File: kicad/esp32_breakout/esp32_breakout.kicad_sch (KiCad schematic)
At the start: 26 parts, among them J1 JST B5B-PH-K-S, J10 JST B6B-PH-K-S, J2 JST B5B-PH-K-S, J3 JST B7B-PH-K-S, J4 XT30U-M, J5 HDR 8p M VERT 2.54mm, J6 JST B5B-ZR, J9 JST B6B-PH-K-S, SW1 SS12D10, U1 ESP32 DEV KIT Module 30-pin, U2 LM2596 Module

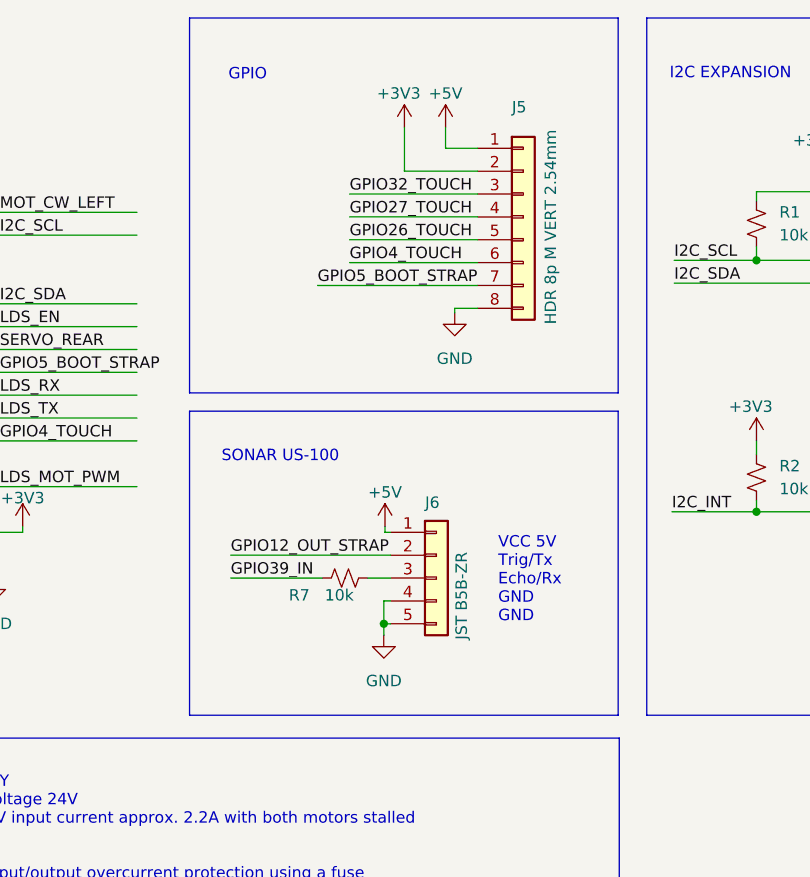
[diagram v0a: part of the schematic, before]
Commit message: Single GPIO header
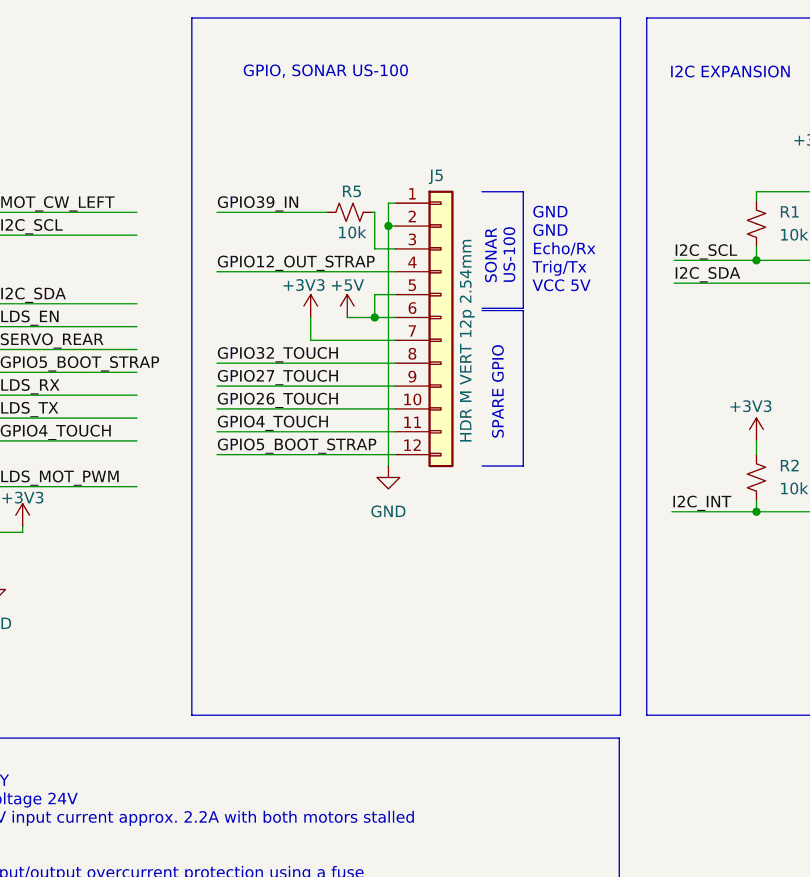
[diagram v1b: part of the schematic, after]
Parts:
- removed J5: HDR 8p M VERT 2.54mm, Connector_PinHeader_2.54mm:PinHeader_1x08_P2.54mm_Vertical, symbol Connector_Generic:Conn_01x08
- removed J6: JST B5B-ZR, Makerspet:JST_ZH_B5B-ZR_1x05_P1.50mm_Vertical, symbol Connector_Generic:Conn_01x05
- removed R7: 10k, Resistor_SMD:R_0603_1608Metric, symbol Device:R_Small_US
- added J5: HDR M VERT 12p 2.54mm, Connector_PinSocket_2.54mm:PinSocket_1x12_P2.54mm_Vertical, symbol Connector_Generic:Conn_01x12
- added R5: 10k, Resistor_SMD:R_0603_1608Metric, symbol Device:R_Small_US
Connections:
- net +3V3: now also J5.7 (Pin_7)
- net +5V: now also J5.5 (Pin_5), J5.6 (Pin_6)
- net GND: now also J5.1 (Pin_1), J5.2 (Pin_2)
- net GPIO12_OUT_STRAP: now also J5.4 (Pin_4)
- net GPIO26_TOUCH: now also J5.10 (Pin_10)
- net GPIO27_TOUCH: now also J5.9 (Pin_9)
- net GPIO32_TOUCH: now also J5.8 (Pin_8)
- net GPIO39_IN: now also R5.1
- net GPIO4_TOUCH: now also J5.11 (Pin_11)
- net GPIO5_BOOT_STRAP: now also J5.12 (Pin_12)
- new net: J5.3 (Pin_3), R5.2
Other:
- note added: "GND GND Echo/Rx Trig/Tx VCC 5V"
- note added: "GPIO, SONAR US-100"
- note added: "SPARE GPIO"
- note removed: "GPIO"
- note removed: "VCC 5V Trig/Tx Echo/Rx GND GND"

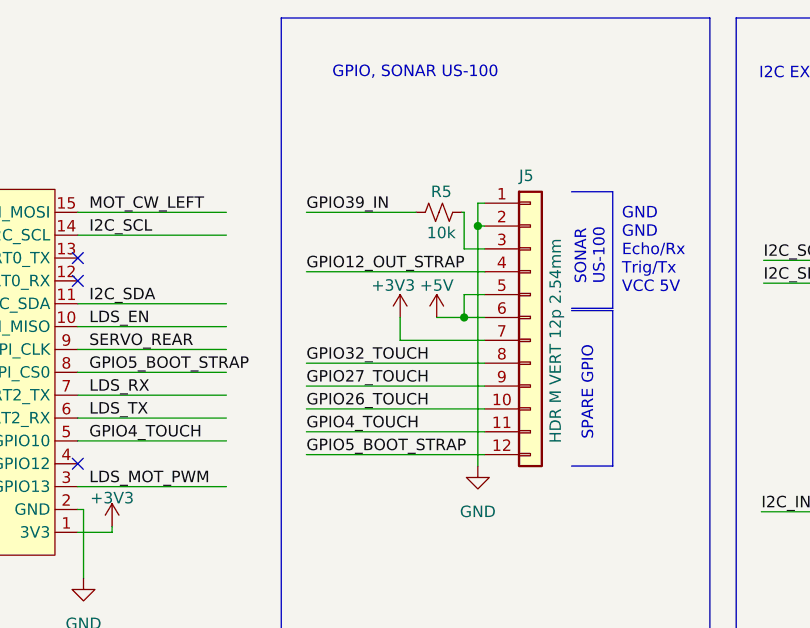
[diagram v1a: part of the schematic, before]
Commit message: PCB hole, sonar tweaks
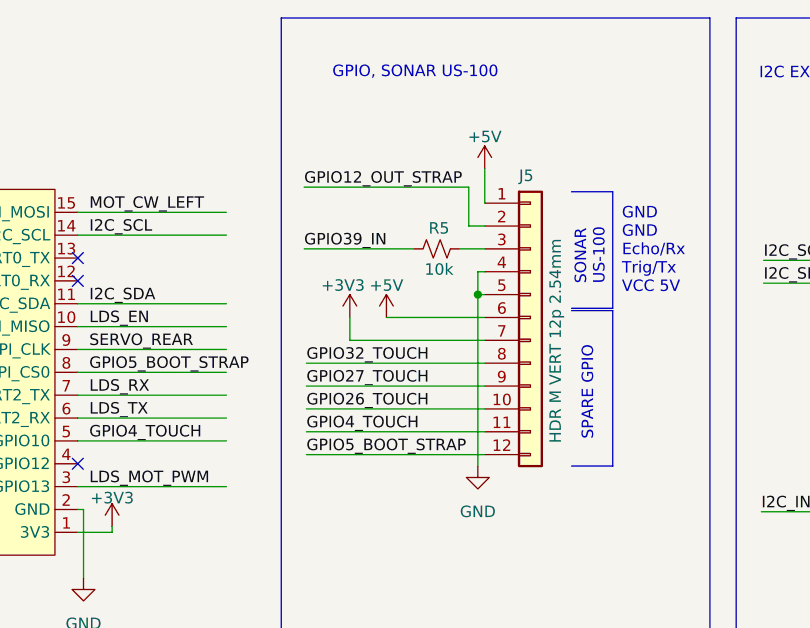
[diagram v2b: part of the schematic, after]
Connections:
- net +5V: now also J5.1 (Pin_1); no longer J5.5 (Pin_5)
- net GND: now also J5.4 (Pin_4), J5.5 (Pin_5); no longer J5.1 (Pin_1), J5.2 (Pin_2)
- net GPIO12_OUT_STRAP: now also J5.2 (Pin_2); no longer J5.4 (Pin_4)
